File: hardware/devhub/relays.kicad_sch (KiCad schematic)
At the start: 17 parts, among them J5 Banana COM 1, J6 Banana NC 1, J7 Banana COM 2, J8 Banana NC 2, K1 G5Q-1 DC5, K2 G5Q-1 DC5, SW1 relè on/off, SW2 relè on/off, U9 ULN2003V12

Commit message: Intial PCB layout
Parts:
- SW1, SW2: footprint Button_Switch_THT:SW_PUSH_6mm_H13mm -> Button_Switch_SMD:SW_SPST_PTS645Sx43SMTR92
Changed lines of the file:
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@@
 			)
 		)
-		(property "Footprint" "Button_Switch_THT:SW_PUSH_6mm_H13mm"
+		(property "Footprint" "Button_Switch_SMD:SW_SPST_PTS645Sx43SMTR92"
 			(at 228.6 121.92 0)
 			(hide yes)
@@
 			)
 		)
-		(property "Footprint" "Button_Switch_THT:SW_PUSH_6mm_H13mm"
+		(property "Footprint" "Button_Switch_SMD:SW_SPST_PTS645Sx43SMTR92"
 			(at 142.24 121.92 0)
 			(hide yes)

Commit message: PCB rules in KiCad, USB pair names, eFuse output bypass and U2 thermal vias (D44-D50)
Stackup JLC04161H-7628, netclasses and custom DRC rules (devhub.kicad_dru) from
docs/regole-pcb.md, with a section for the checks that DRC cannot cover. C7 1 uF on
the TPS259470A output before the shunt (D48). USB nets renamed to DP/DN so KiCad
recognizes the differential pairs (D49). U2 footprint with 0.3 mm thermal vias, open
on both sides for the prototype; encroached vias and a JLCPCB order note for
production (D50). Also includes stock part codes, cost comparison and placement rules
(D44-D47).
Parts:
- C81, C82: digikey (none) -> 1276-1003-1-ND; lcsc (none) -> C83055; mouser (none) -> 187-CL21B104KBCNNNC; warehouse (none) -> 178
- C83, C84: digikey (none) -> 1276-1000-1-ND; lcsc (none) -> C1591; mouser (none) -> 187-CL10B104KB8NNNC; warehouse (none) -> 235
- J5, J7: digikey (none) -> 4654-FCR7350B-ND
- J6, J8: digikey (none) -> 4654-FCR7350R-ND; lcsc (none) -> C6041087
- K1, K2: digikey (none) -> Z12713-ND; lcsc (none) -> C397241; mouser (none) -> 653-G5Q-1-DC5
- R81, R82: digikey (none) -> 311-100FRCT-ND; lcsc (none) -> C137392; mouser (none) -> 603-RC1206FR-07100RL
- SW1, SW2: digikey (none) -> CKN10820CT-ND; lcsc (none) -> C285485; mouser (none) -> 611-645SL70SMTR92LFS
- U9: digikey (none) -> 296-30538-1-ND; lcsc (none) -> C94916; mouser (none) -> 595-ULN2003V12DR

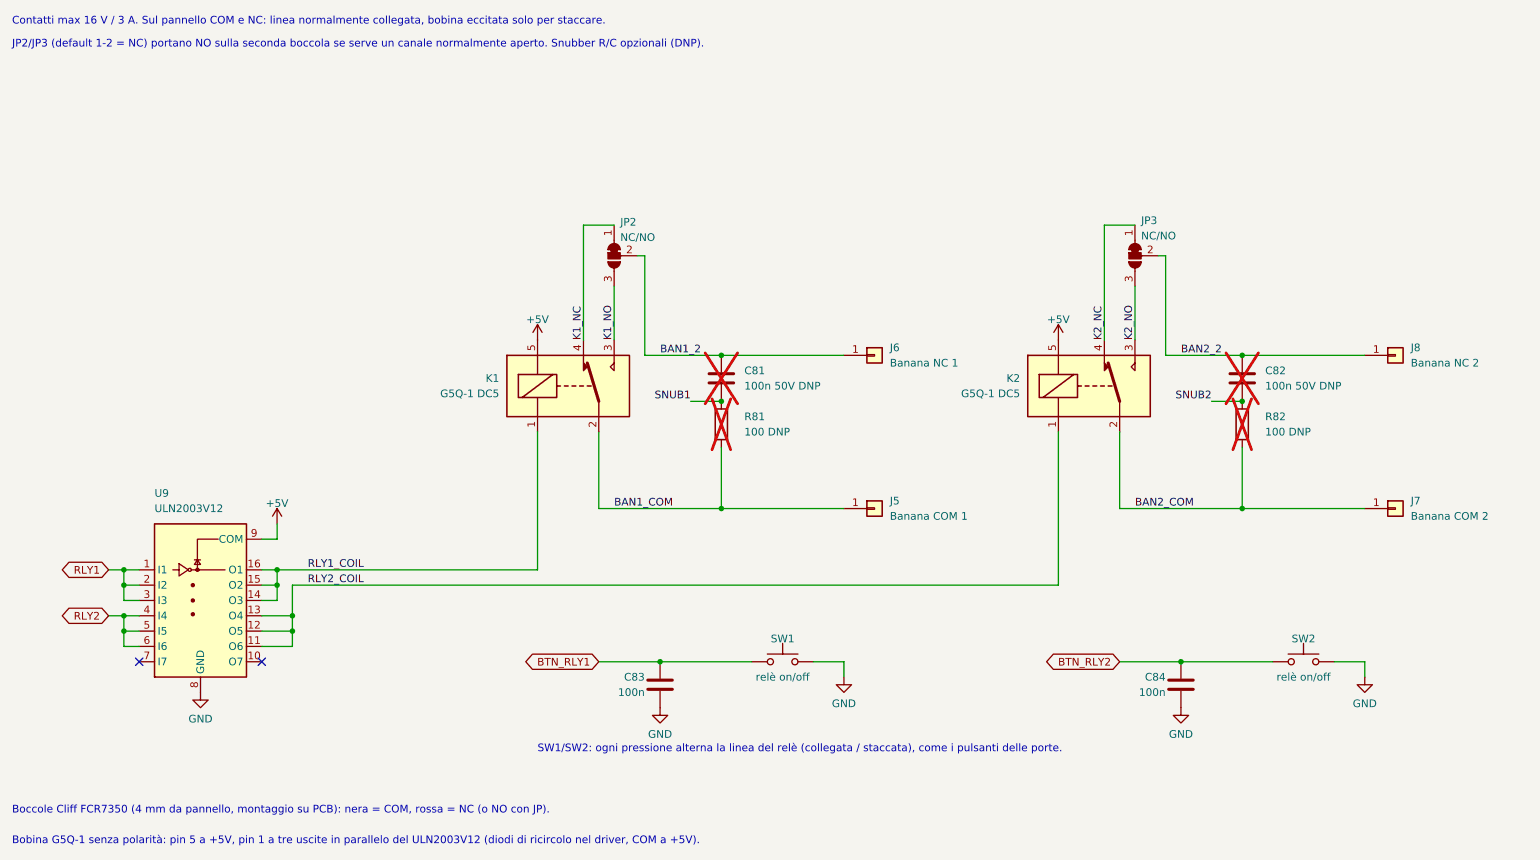
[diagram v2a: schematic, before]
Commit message: Schematic v0.3: apply simplified requirements (D79-D81)
Update the existing KiCad project instead of starting over:
- MCU U3 replaced with STM32G0B1CEU6 (UFQFPN48) on the 48-pin pinout
- switches sheet: two UCS2114-1-V/LX on separate I2C buses replace
  TPS2561A, INA3221 and current shunts
- ports: single MCU-driven LED, discrete VBUS discharge removed
- remove USB-A port, spare hub header, second relay channel,
  input CC ADC filters and input shunt
- add UCS2114 symbol and footprint (Microchip land pattern C04-2421)
- align pinout, decisions, architecture and component docs
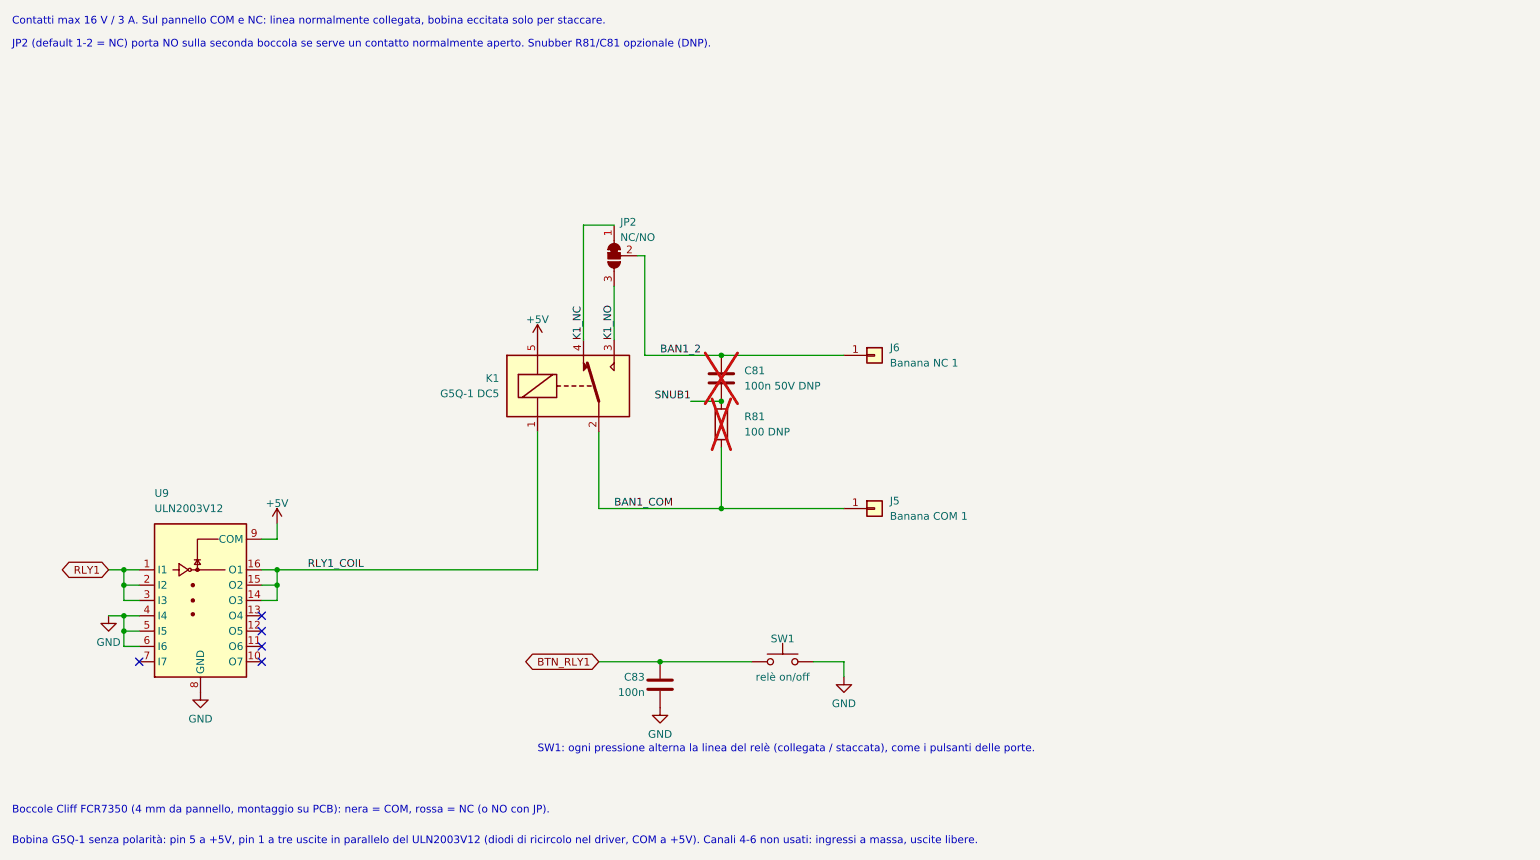
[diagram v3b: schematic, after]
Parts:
- removed C82: 100n 50V DNP, Capacitor_SMD:C_0805_2012Metric, symbol Device:C
- removed C84: 100n, Capacitor_SMD:C_0603_1608Metric, symbol Device:C
- removed J7: Banana COM 2, Connector:Banana_Cliff_FCR7350B_S16N-PC_Horizontal, symbol Connector_Generic:Conn_01x01
- removed J8: Banana NC 2, Connector:Banana_Cliff_FCR7350R_S16N-PC_Horizontal, symbol Connector_Generic:Conn_01x01
- removed JP3: NC/NO, Jumper:SolderJumper-3_P1.3mm_Bridged12_RoundedPad1.0x1.5mm, symbol Jumper:SolderJumper_3_Bridged12
- removed K2: G5Q-1 DC5, Relay_THT:Relay_SPDT_Omron-G5Q-1, symbol Relay:G5Q-1
- removed R82: 100 DNP, Resistor_SMD:R_1206_3216Metric, symbol Device:R
- removed SW2: relè on/off, Button_Switch_SMD:SW_SPST_PTS645Sx43SMTR92, symbol Switch:SW_Push
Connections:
- net RLY2 is gone; now on net GND: U9.4 (I4), U9.5 (I5), U9.6 (I6)
- removed net RLY2_COIL: U9.11 (O6), U9.12 (O5), U9.13 (O4)
- no-connect marks 2 -> 5
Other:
- note added: "Bobina G5Q-1 senza polarità: pin 5 a +5V, pin 1 a tre uscite in parallelo del ULN2003V12 (diodi di ricircolo nel driver, COM a +5V). Canali 4-6 non usati: ingressi a massa, uscite libere."
- note added: "JP2 (default 1-2 = NC) porta NO sulla seconda boccola se serve un contatto normalmente aperto. Snubber R81/C81 opzionale (DNP)."
- note added: "SW1: ogni pressione alterna la linea del relè (collegata / staccata), come i pulsanti delle porte."
- note removed: "Bobina G5Q-1 senza polarità: pin 5 a +5V, pin 1 a tre uscite in parallelo del ULN2003V12 (diodi di ricircolo nel driver, COM a +5V)."
- note removed: "JP2/JP3 (default 1-2 = NC) portano NO sulla seconda boccola se serve un canale normalmente aperto. Snubber R/C opzionali (DNP)."
- note removed: "SW1/SW2: ogni pressione alterna la linea del relè (collegata / staccata), come i pulsanti delle porte."
- title: Relè ausiliari su boccole a banana -> Relè ausiliario su boccole a banana

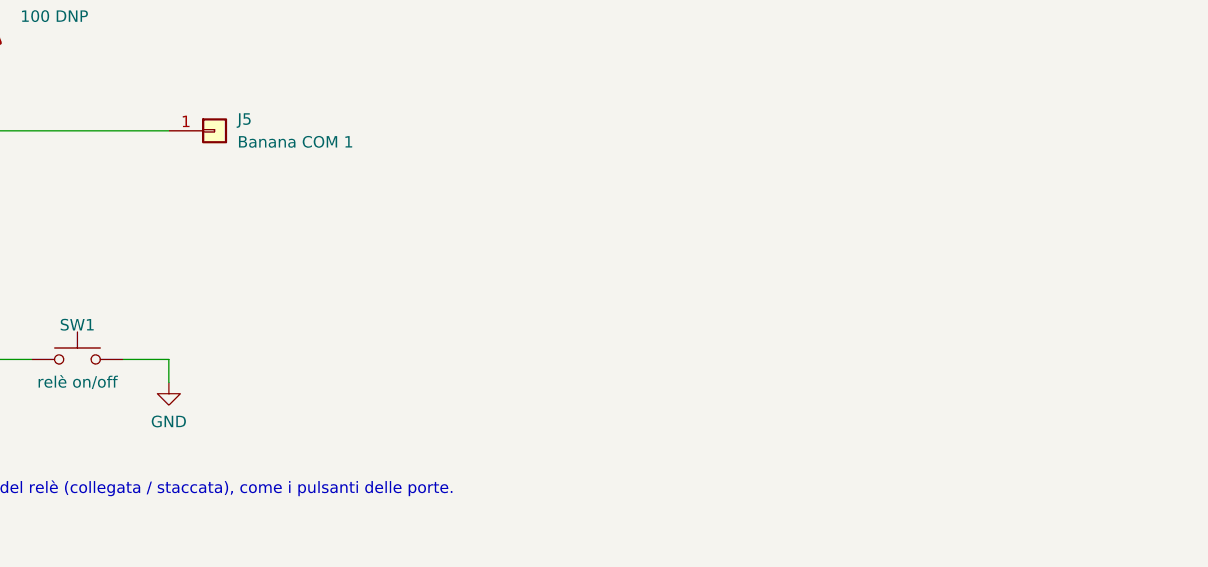
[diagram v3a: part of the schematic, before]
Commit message: Restore relay LED, larger NC/NO jumper, PCB routing progress (D89, D90)
- D90/R90 relay LED back on RLY1, in the front LED row in line with SW1;
  host LED D93/R93 moved to the rear next to J1
- JP2: project footprint with 2.0x3.0 mm pads, 2.4 mm pitch and 1.0 mm
  bridge for 3 A relay contacts
- U13: 0.2 mm tracks from pads 8/9 alongside the corner pads, no clearance
  exception
- Routing and placement progress, zone defaults, schematic layout cleanup
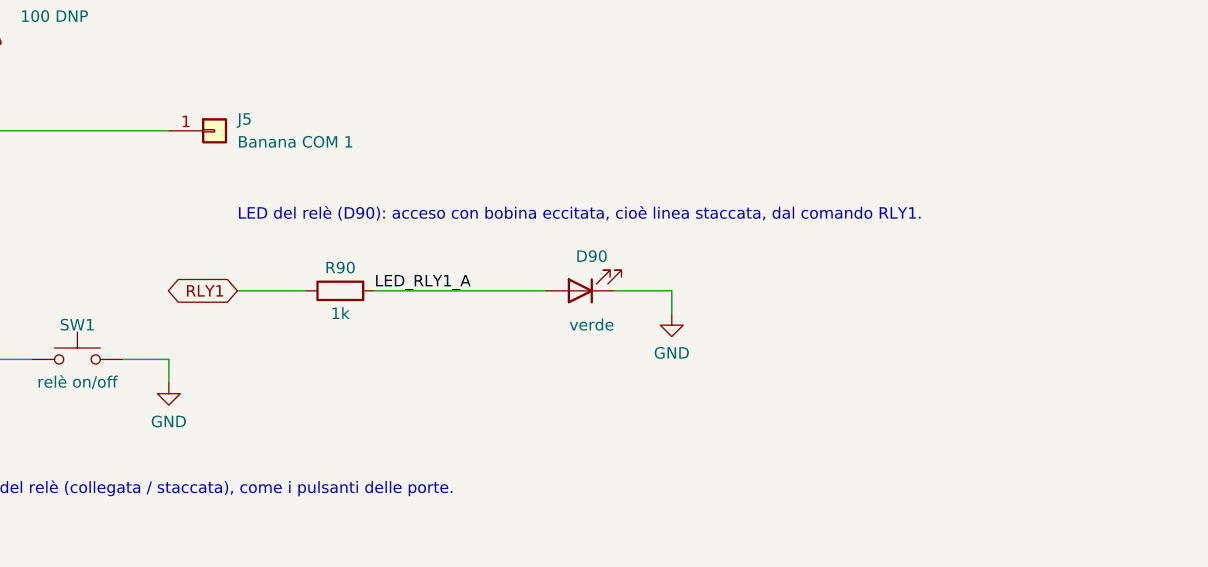
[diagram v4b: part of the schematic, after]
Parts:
- added D90: verde, LED_SMD:LED_0805_2012Metric, symbol Device:LED
- added R90: 1k, Resistor_SMD:R_0603_1608Metric, symbol Device:R
- JP2: footprint Jumper:SolderJumper-3_P1.3mm_Bridged12_RoundedPad1.0x1.5mm -> lcsc_footprints:SolderJumper-3_P2.4mm_Bridged12_Pad2.0x3.0mm
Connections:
- net GND: now also D90.1 (K)
- net RLY1: now also R90.1
- new net LED_RLY1_A: D90.2 (A), R90.2
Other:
- note added: "LED del relè (D90): acceso con bobina eccitata, cioè linea staccata, dal comando RLY1."

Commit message: PCB routing complete, package in values, MPN fields
- Routing finished; ESD_FANOUT rule area for D20 centre pins
- Vias keep inner-layer rings only where connected; GND reference vias
  next to SWD and I2C layer changes
- Value field of chip R/C/LED includes the package (0402...1206)
- New fields MPN lcsc, MPN mouser, MPN digikey; LCSC codes for R60/R61,
  U3, U4/U5 and supplier codes completed; JP2 marked DNP on the PCB
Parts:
- C81: value 100n 50V DNP -> 100n 50V 0805 DNP; MPN digikey (none) -> CL21B104KBCNNNC; MPN lcsc (none) -> 0805B104K500CT; MPN mouser (none) -> CL21B104KBCNNNC
- C83: value 100n -> 100n 0603; MPN digikey (none) -> CL10B104KB8NNNC; MPN lcsc (none) -> CL10B104KB8NNNC; MPN mouser (none) -> CL10B104KB8NNNC
- D90: value verde -> verde 0805; MPN digikey (none) -> LTST-C171GKT; MPN lcsc (none) -> LTST-C171GKT; MPN mouser (none) -> LTST-C171GKT
- J5: MPN digikey (none) -> FCR7350B
- J6: MPN digikey (none) -> FCR7350R; MPN lcsc (none) -> FCR7350R
- JP2: now not fitted
- K1: MPN digikey (none) -> G5Q-1 DC5; MPN lcsc (none) -> G5Q-14 DC5; MPN mouser (none) -> G5Q-1 DC5
- R81: value 100 DNP -> 100 0.25W 1206 DNP; MPN digikey (none) -> RC1206FR-07100RL; MPN lcsc (none) -> RC1206FR-07100RL; MPN mouser (none) -> RC1206FR-07100RL
- R90: value 1k -> 1k 0603; MPN digikey (none) -> RC0603FR-071KL; MPN lcsc (none) -> 0603WAF1001T5E; MPN mouser (none) -> RC0603FR-071KL
- SW1: MPN digikey (none) -> PTS645SL70SMTR92 LFS; MPN lcsc (none) -> PTS645SL70SMTR92 LFS; MPN mouser (none) -> PTS645SL70SMTR92 LFS
- U9: MPN digikey (none) -> ULN2003V12DR; MPN lcsc (none) -> ULN2003V12DR; MPN mouser (none) -> ULN2003V12DR

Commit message: Test points, LED host moved, board finished (D92)
- 14 test points: GND loops TP1/TP10 (Keystone 5001), pads for +5V, +3V3,
  I2C1/I2C2, HUB_RST_N, EFUSE_FLT_N and VBUS_P1-P4
- D93/R93 moved to the rear, left of J1
- Button symbols: generic Value, function in Description; PCB aligned
- Docs: decision D92, components, PCB test rules, LED host position
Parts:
- SW1: value relè on/off -> Push button switch, generic, two pins
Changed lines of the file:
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@@
 			)
 		)
-		(property "Value" "relè on/off"
+		(property "Value" "Push button switch, generic, two pins"
 			(at 142.24 124.46 0)
 			(show_name no)
@@
 			)
 		)
-		(property "Description" "Push button switch, generic, two pins"
+		(property "Description" "relè on/off"
 			(at 142.24 121.92 0)
 			(hide yes)
